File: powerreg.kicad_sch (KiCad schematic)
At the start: 76 parts, among them J21 USB_C_Receptacle_USB2.0_16P, Q18 SQJ407EP-T1_GE3, Q19 SQJ407EP-T1_GE3, U11 AP22811AW5-7, U3 TPS54531DDAR, U5 TPS54331DR, U6 2920L500/30GR, U8 TPS54331DR

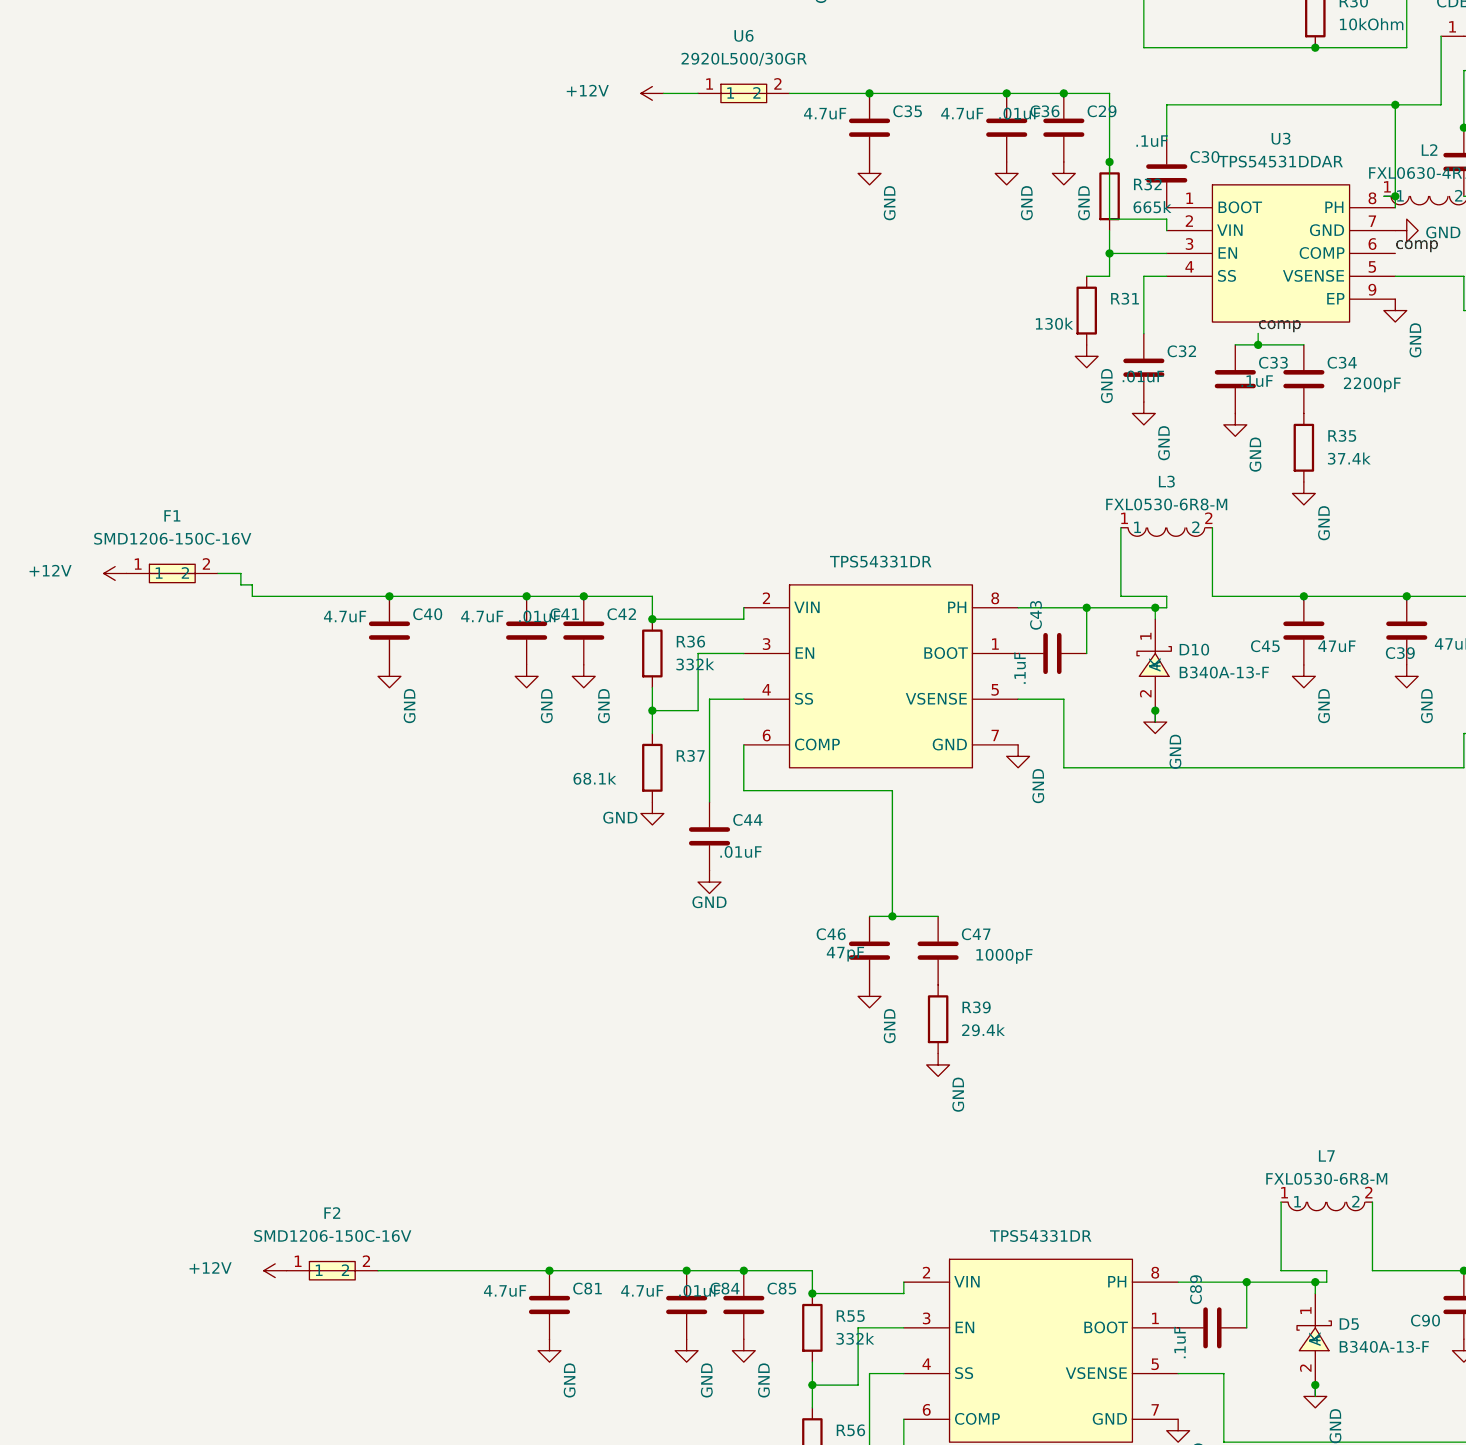
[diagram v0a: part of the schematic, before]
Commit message: Updated schematic and routed PCB traces
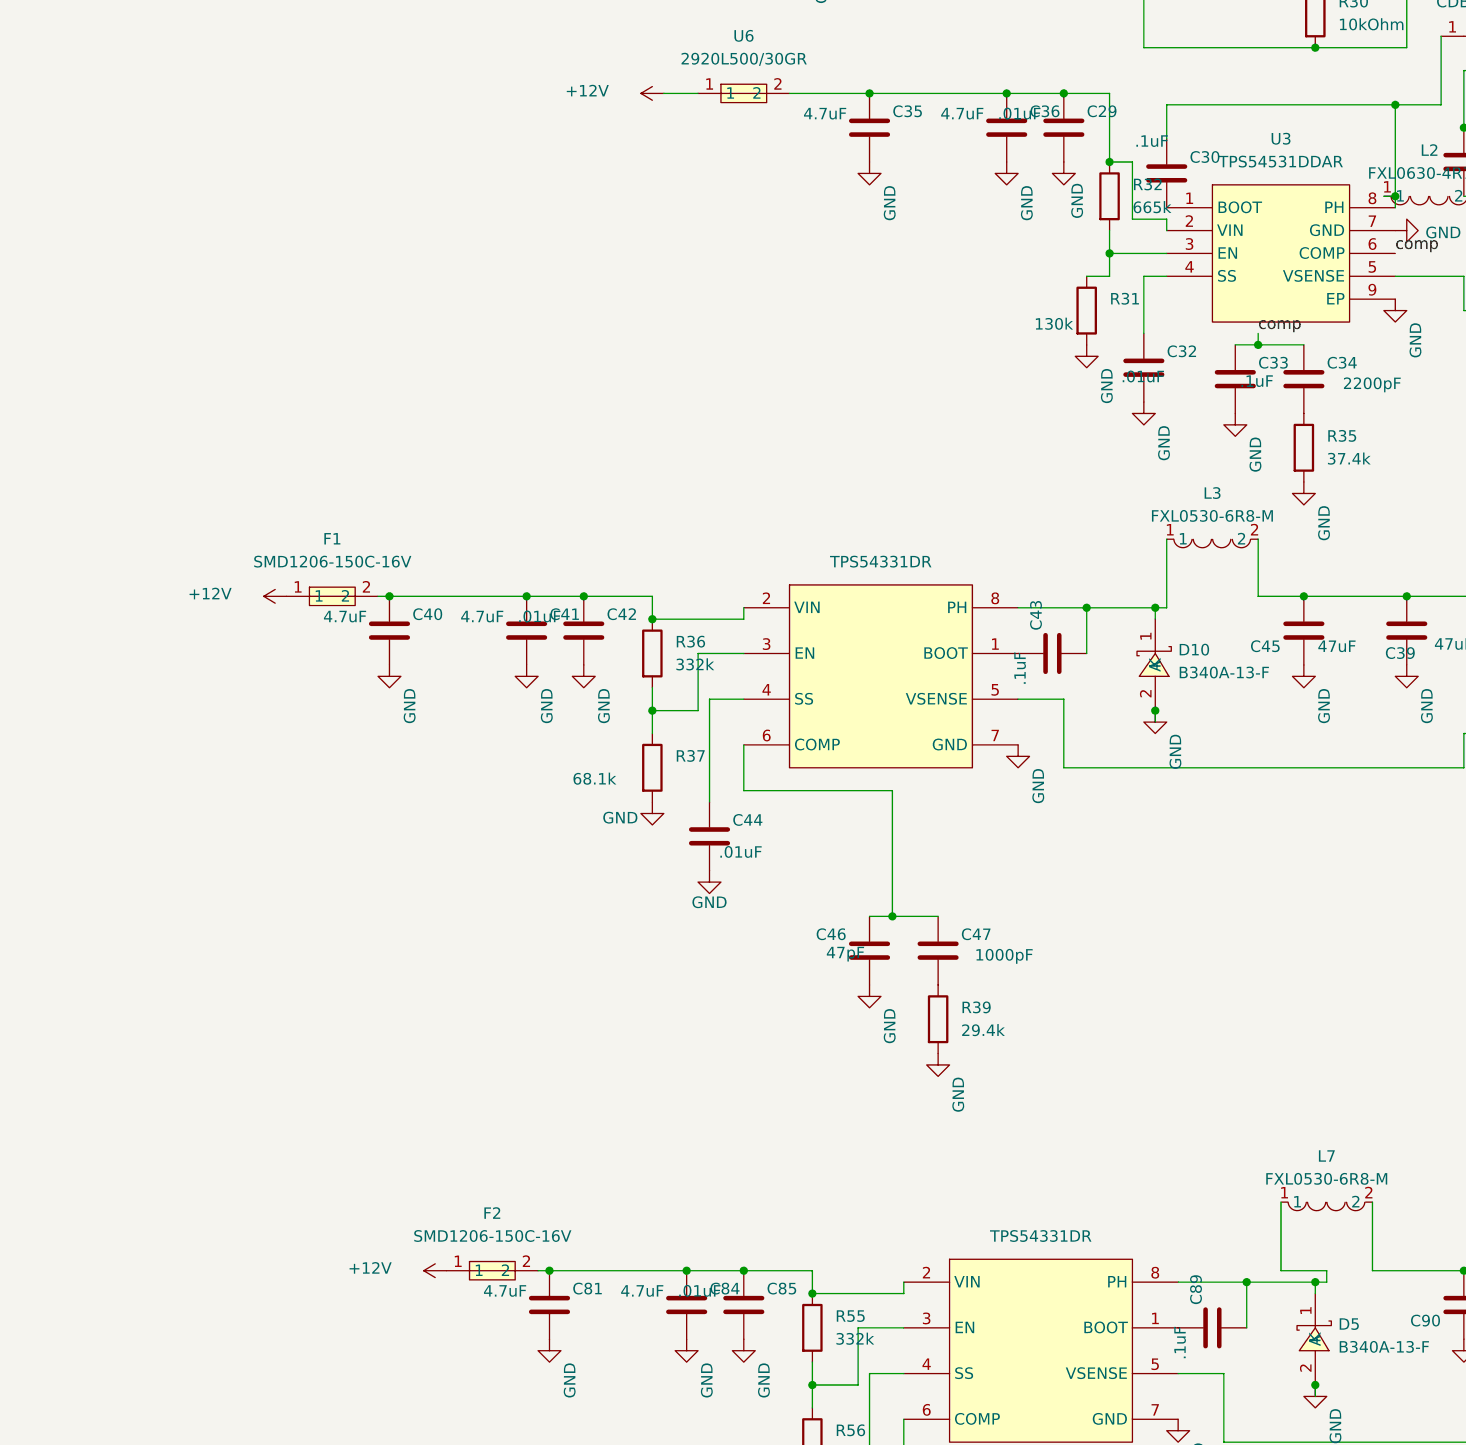
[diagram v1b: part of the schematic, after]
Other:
- moved on the sheet: F1, F2, L3
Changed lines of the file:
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@@
 	(wire
 		(pts
-			(xy 146.05 80.01) (xy 139.7 80.01)
+			(xy 146.05 80.01) (xy 142.24 80.01)
 		)
 		(stroke
@@
 	(wire
 		(pts
-			(xy 139.7 73.66) (xy 139.7 80.01)
+			(xy 142.24 73.66) (xy 142.24 80.01)
 		)
 		(stroke
@@
 	(wire
 		(pts
-			(xy 43.18 120.65) (xy 44.45 120.65)
-		)
-		(stroke
-			(width 0)
-			(type default)
-		)
-	)
-	(wire
-		(pts
 			(xy 162.56 210.82) (xy 162.56 209.55)
 		)
@@
 	(wire
 		(pts
-			(xy 40.64 119.38) (xy 43.18 119.38)
+			(xy 58.42 121.92) (xy 59.69 121.92)
 		)
 		(stroke
@@
 	(wire
 		(pts
-			(xy 44.45 121.92) (xy 59.69 121.92)
-		)
-		(stroke
-			(width 0)
-			(type default)
-		)
-	)
-	(wire
-		(pts
 			(xy 111.76 203.2) (xy 116.84 203.2)
 		)
@@
 	(wire
 		(pts
-			(xy 140.97 121.92) (xy 146.05 121.92)
-		)
-		(stroke
-			(width 0)
-			(type default)
-		)
-	)
-	(wire
-		(pts
 			(xy 152.4 39.37) (xy 152.4 35.56)
 		)
@@
 	(wire
 		(pts
-			(xy 44.45 120.65) (xy 44.45 121.92)
-		)
-		(stroke
-			(width 0)
-			(type default)
-		)
-	)
-	(wire
-		(pts
 			(xy 269.24 220.98) (xy 269.24 222.25)
 		)
@@
 	(wire
 		(pts
-			(xy 146.05 123.19) (xy 146.05 121.92)
+			(xy 146.05 115.57) (xy 146.05 123.19)
 		)
 		(stroke
@@
 	(wire
 		(pts
-			(xy 43.18 119.38) (xy 43.18 120.65)
-		)
-		(stroke
-			(width 0)
-			(type default)
-		)
-	)
-	(wire
-		(pts
 			(xy 133.35 218.44) (xy 133.35 232.41)
 		)
@@
 	(wire
 		(pts
-			(xy 137.16 123.19) (xy 137.16 128.27)
+			(xy 142.24 73.66) (xy 139.7 73.66)
 		)
 		(stroke
@@
 	(wire
 		(pts
-			(xy 140.97 114.3) (xy 140.97 121.92)
+			(xy 137.16 123.19) (xy 137.16 128.27)
 		)
 		(stroke
@@
 	(wire
 		(pts
-			(xy 58.42 196.85) (xy 77.47 196.85)
+			(xy 76.2 196.85) (xy 77.47 196.85)
 		)
 		(stroke
@@
 	(wire
 		(pts
-			(xy 151.13 114.3) (xy 151.13 121.92)
+			(xy 156.21 115.57) (xy 156.21 121.92)
 		)
 		(stroke
@@
 	(wire
 		(pts
-			(xy 151.13 121.92) (xy 161.29 121.92)
+			(xy 156.21 121.92) (xy 161.29 121.92)
 		)
 		(stroke
@@
 	(symbol
 		(lib_id "easyeda2kicad:FXL0530-6R8-M")
-		(at 146.05 114.3 0)
+		(at 151.13 115.57 0)
 		(unit 1)
 		(exclude_from_sim no)
@@
 		(fields_autoplaced yes)
 		(property "Reference" "L3"
-			(at 146.05 109.22 0)
+			(at 151.13 110.49 0)
 			(effects
 				(font
@@
 		)
 		(property "Value" "FXL0530-6R8-M"
-			(at 146.05 111.76 0)
+			(at 151.13 113.03 0)
 			(effects
 				(font
@@
 		)
 		(property "Footprint" "easyeda2kicad:IND-SMD_L5.4-W5.2_FXL0530"
-			(at 146.05 121.92 0)
+			(at 151.13 123.19 0)
 			(effects
 				(font
@@
 		)
 		(property "Datasheet" "https://lcsc.com/product-detail/Others_6-8uH-20_C177249.html"
-			(at 146.05 124.46 0)
+			(at 151.13 125.73 0)
 			(effects
 				(font
@@
 		)
 		(property "Description" ""
-			(at 146.05 114.3 0)
+			(at 151.13 115.57 0)
 			(effects
 				(font
@@
 		)
 		(property "LCSC Part" "C177249"
-			(at 146.05 127 0)
+			(at 151.13 128.27 0)
 			(effects
 				(font
@@
 		)
 		(property "Value" "GND"
-			(at 136.906 78.232 90)
+			(at 136.144 77.978 90)
 			(effects
 				(font
@@
 	(symbol
 		(lib_id "easyeda2kicad:SMD1206-150C-16V")
-		(at 35.56 119.38 0)
+		(at 53.34 121.92 0)
 		(unit 1)
 		(exclude_from_sim no)
@@
 		(fields_autoplaced yes)
 		(property "Reference" "F1"
-			(at 35.56 113.03 0)
+			(at 53.34 115.57 0)
 			(effects
 				(font
@@
 		)
 		(property "Value" "SMD1206-150C-16V"
-			(at 35.56 115.57 0)
+			(at 53.34 118.11 0)
 			(effects
 				(font
@@
 		)
 		(property "Footprint" "easyeda2kicad:F1206"
-			(at 35.56 127 0)
+			(at 53.34 129.54 0)
 			(effects
 				(font
@@
 		)
 		(property "Datasheet" ""
-			(at 35.56 119.38 0)
+			(at 53.34 121.92 0)
 			(effects
 				(font
@@
 		)
 		(property "Description" ""
-			(at 35.56 119.38 0)
+			(at 53.34 121.92 0)
 			(effects
 				(font
@@
 		)
 		(property "LCSC Part" "C2760275"
-			(at 35.56 129.54 0)
+			(at 53.34 132.08 0)
 			(effects
 				(font
@@
 	(symbol
 		(lib_id "power:+12V")
-		(at 48.26 196.85 90)
+		(at 66.04 196.85 90)
 		(unit 1)
 		(exclude_from_sim no)
@@
 		(dnp no)
 		(property "Reference" "#PWR0226"
-			(at 52.07 196.85 0)
+			(at 69.85 196.85 0)
 			(effects
 				(font
@@
 		)
 		(property "Value" "+12V"
-			(at 42.164 196.596 90)
+			(at 59.944 196.596 90)
 			(effects
 				(font
@@
 		)
 		(property "Footprint" ""
-			(at 48.26 196.85 0)
+			(at 66.04 196.85 0)
 			(effects
 				(font
@@
 		)
 		(property "Datasheet" ""
-			(at 48.26 196.85 0)
+			(at 66.04 196.85 0)
 			(effects
 				(font
@@
 		)
 		(property "Description" "Power symbol creates a global label with name \"+12V\""
-			(at 48.26 196.85 0)
+			(at 66.04 196.85 0)
 			(effects
 				(font
@@
 	(symbol
 		(lib_id "easyeda2kicad:SMD1206-150C-16V")
-		(at 53.34 196.85 0)
+		(at 71.12 196.85 0)
 		(unit 1)
 		(exclude_from_sim no)
@@
 		(fields_autoplaced yes)
 		(property "Reference" "F2"
-			(at 53.34 190.5 0)
+			(at 71.12 190.5 0)
 			(effects
 				(font
@@
 		)
 		(property "Value" "SMD1206-150C-16V"
-			(at 53.34 193.04 0)
+			(at 71.12 193.04 0)
 			(effects
 				(font
@@
 		)
 		(property "Footprint" "easyeda2kicad:F1206"
-			(at 53.34 204.47 0)
+			(at 71.12 204.47 0)
 			(effects
 				(font
@@
 		)
 		(property "Datasheet" ""
-			(at 53.34 196.85 0)
+			(at 71.12 196.85 0)
 			(effects
 				(font
@@
 		)
 		(property "Description" ""
-			(at 53.34 196.85 0)
+			(at 71.12 196.85 0)
 			(effects
 				(font
@@
 		)
 		(property "LCSC Part" "C2760275"
-			(at 53.34 207.01 0)
+			(at 71.12 207.01 0)
 			(effects
 				(font
@@
 	(symbol
 		(lib_id "power:+12V")
-		(at 30.48 119.38 90)
+		(at 48.26 121.92 90)
 		(unit 1)
 		(exclude_from_sim no)
@@
 		(dnp no)
 		(property "Reference" "#PWR089"
-			(at 34.29 119.38 0)
+			(at 52.07 121.92 0)
 			(effects
 				(font
@@
 		)
 		(property "Value" "+12V"
-			(at 24.384 119.126 90)
+			(at 42.164 121.666 90)
 			(effects
 				(font
@@
 		)
 		(property "Footprint" ""
-			(at 30.48 119.38 0)
+			(at 48.26 121.92 0)
 			(effects
 				(font
@@
 		)
 		(property "Datasheet" ""
-			(at 30.48 119.38 0)
+			(at 48.26 121.92 0)
 			(effects
 				(font
@@
 		)
 		(property "Description" "Power symbol creates a global label with name \"+12V\""
-			(at 30.48 119.38 0)
+			(at 48.26 121.92 0)
 			(effects
 				(font

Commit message: Updated schematic and routed PCB
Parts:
- removed D6: TPD2EUSB30ADRTR, easyeda2kicad:SOT-9X3-3_L1.0-W0.8-P0.35-LS1.0-BR, symbol easyeda2kicad:TPD2EUSB30ADRTR
- removed J21: USB_C_Receptacle_USB2.0_16P, Connector_USB:USB_C_Receptacle_HRO_TYPE-C-31-M-12, symbol Connector:USB_C_Receptacle_USB2.0_16P
- removed R42, R43: 5.1k, Resistor_SMD:R_0603_1608Metric, symbol Device:R
- removed R62, R63: 22, Resistor_SMD:R_0603_1608Metric, symbol Device:R
- removed U11: AP22811AW5-7, easyeda2kicad:SOT-25-5_L3.0-W1.6-P0.95-LS2.8-BL, symbol easyeda2kicad:AP22811AW5-7
